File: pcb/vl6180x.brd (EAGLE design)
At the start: 8.3 x 13.3 mm, 5 parts, among them J1 6PINBOARDEDGE, U1 STPROXSENSOR

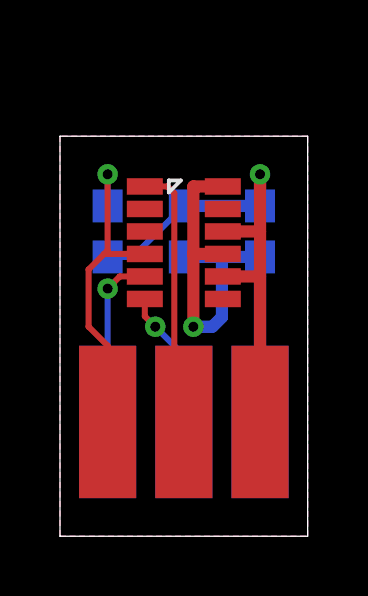
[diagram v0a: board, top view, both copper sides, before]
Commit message: Added pin labels to proximity sensor board
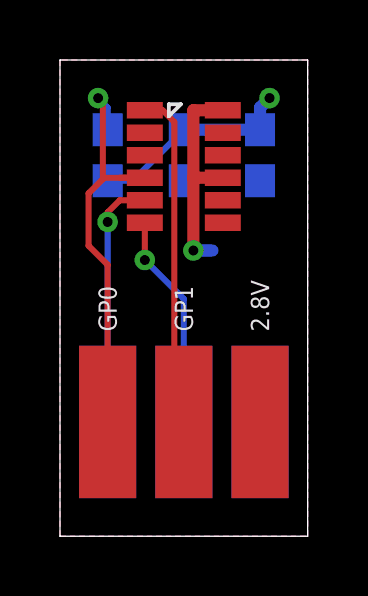
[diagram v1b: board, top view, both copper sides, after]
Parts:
- moved C1 2.54 mm to (6.67, 12.7)
- moved C2 2.54 mm to (4.13, 12.7)
- moved R1 2.54 mm to (1.59, 12.7)
- moved U1 2.54 mm to (4.13, 12.7)
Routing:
- net 2.8V: track 17.6 -> 6.97 mm
- net GND: track 17.8 -> 7.27 mm
- net N$1: track 12.0 -> 14.7 mm
- net N$2: track 5.85 -> 8.39 mm
- net N$3: track 4.64 -> 7.18 mm
- net N$4: track 9.02 -> 11.2 mm
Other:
- board size 8.3 x 13.3 mm -> 8.3 x 15.9 mm
- board text added: "2.8V"
- board text added: "GND"
- board text added: "GP0"
- board text added: "GP1"
- board text added: "SCL"
- board text added: "SDA"
